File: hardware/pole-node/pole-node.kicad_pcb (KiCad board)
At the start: 2 copper layers, 50.5 x 33.5 mm, 31 parts, among them J1 Anderson, J2 RJ45, J3 Conn_01x02, J4 Conn_01x03, J5 Conn_01x03, J6 Conn_01x03, U1 AP3211, U2 MAX485E, U3 MAX485E

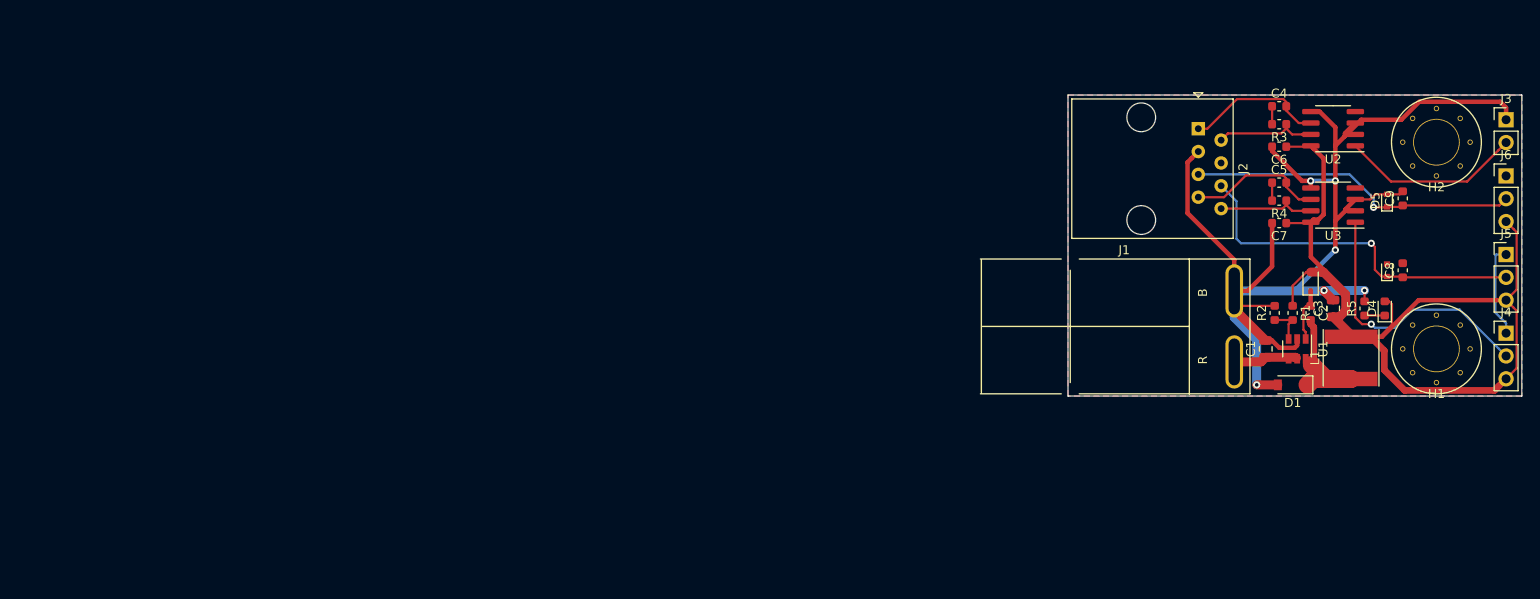
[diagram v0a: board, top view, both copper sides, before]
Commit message: Update pole node to v1.1
This adds lots of TVS diode, more decoupling, bulk caps on 5v and 12v
lines. Also adds pass-through Anderson connector.
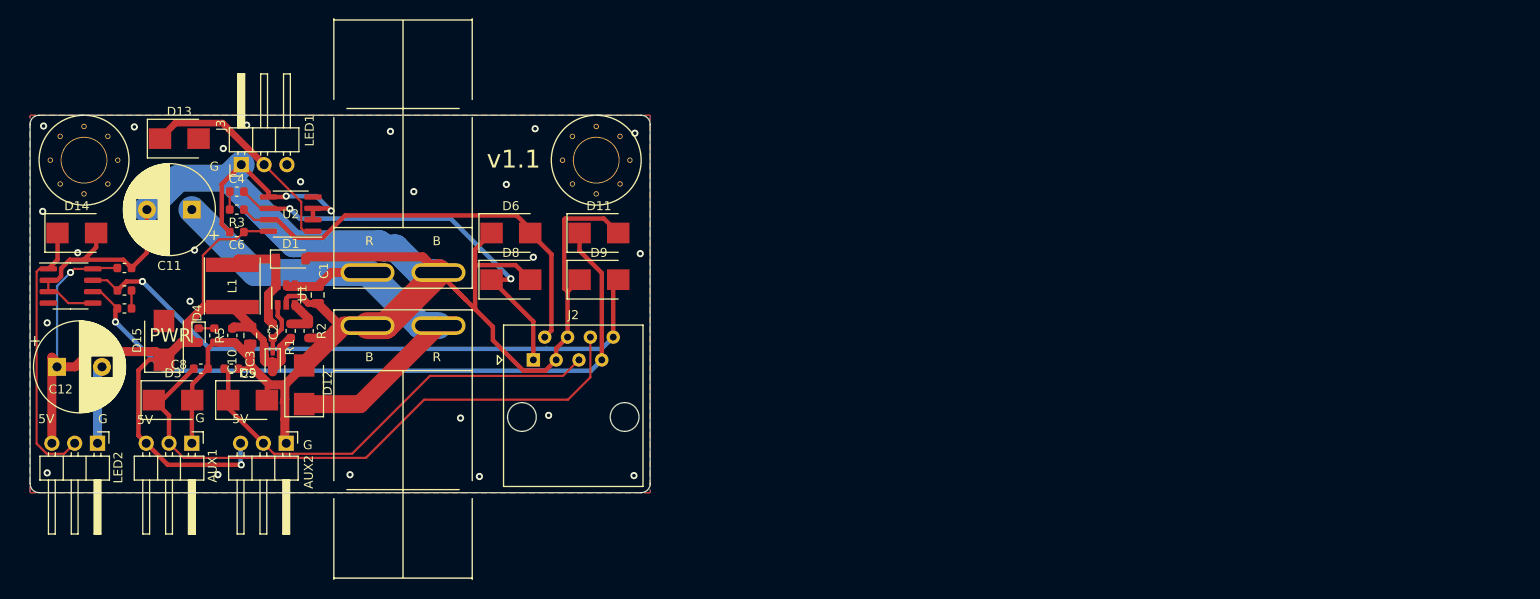
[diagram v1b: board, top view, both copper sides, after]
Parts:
- added C10: .1uF, Capacitor_SMD:C_0603_1608Metric, F.Cu at (60.0, 60.0)
- added C11: 470uF, Capacitor_THT:CP_Radial_D10.0mm_P5.00mm, F.Cu at (55.5, 46.0)
- added C12: 470uF, Capacitor_THT:CP_Radial_D10.0mm_P5.00mm, F.Cu at (40.5, 63.5)
- added D11: D_TVS_DATA, Diode_SMD:D_SMB, F.Cu at (100.8, 48.6)
- added D12: D_TVS_12V, Diode_SMD:D_SMB, F.Cu at (68.0, 65.5)
- added D13: D_TVS_5V, Diode_SMD:D_SMB, F.Cu at (54.1, 38.1)
- added D14: D_TVS_5V, Diode_SMD:D_SMB, F.Cu at (42.7, 48.6)
- added D15: D_TVS_5V, Diode_SMD:D_SMB, F.Cu at (52.4, 60.5)
- added D6: D_TVS_DATA, Diode_SMD:D_SMB, F.Cu at (91.0, 48.6)
- added D8: D_TVS_DATA, Diode_SMD:D_SMB, F.Cu at (91.0, 53.8)
- added D9: D_TVS_DATA, Diode_SMD:D_SMB, F.Cu at (100.8, 53.8)
- added J7: Anderson, homebrew:Anderson_1336G1_right_angle_bottom_two, F.Cu at (79.0, 53.0)
- D3, D5: value D_TVS -> D_TVS_5V; footprint Diode_SMD:D_SOD-523 -> Diode_SMD:D_SMB
- J1: footprint homebrew:Anderson_1337G3_right_angle_bottom_two -> homebrew:Anderson_1336G1_right_angle_bottom_two
- J3: value Conn_01x02 -> Conn_01x03; footprint Connector_PinHeader_2.54mm:PinHeader_1x02_P2.54mm_Vertical -> Connector_PinHeader_2.54mm:PinHeader_1x03_P2.54mm_Horizontal
- J4, J5, J6: footprint Connector_PinHeader_2.54mm:PinHeader_1x03_P2.54mm_Vertical -> Connector_PinHeader_2.54mm:PinHeader_1x03_P2.54mm_Horizontal
- moved J4 157.2 mm to (45.0, 72.0), turned to 270 degrees
- moved H1 152.0 mm to (43.5, 40.5)
- moved J5 147.8 mm to (55.5, 72.0), turned to 270 degrees
- moved J3 140.8 mm to (61.0, 41.0), turned to 90 degrees
- moved U3 140.8 mm to (42.0, 54.5), turned to 0 degrees
- moved J6 139.0 mm to (66.0, 72.0), turned to 270 degrees
- moved D3 135.9 mm to (53.4, 67.2), turned to 0 degrees
- moved C8 134.2 mm to (56.5, 63.7), turned to 0 degrees
- moved D4 132.0 mm to (56.2, 60.0), turned to 270 degrees
- moved C9 131.7 mm to (59.9, 63.7), turned to 0 degrees
- moved C5 129.3 mm to (48.0, 57.0), turned to 180 degrees
- moved R4 128.9 mm to (48.0, 55.0), turned to 0 degrees
- moved D5 128.7 mm to (61.7, 67.2), turned to 0 degrees
- moved C7 128.6 mm to (48.0, 52.5), turned to 0 degrees
- moved R5 128.0 mm to (58.0, 60.0), turned to 270 degrees
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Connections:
- net Net-(C1-Pad1) renamed +12V
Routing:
- net GND: track 162.9 -> 250.8 mm, vias 6 -> 26
- net LED_2_A: track 15.2 -> 77.1 mm, vias 0 -> 1
- net LED_2_B: track 10.9 -> 69.1 mm, vias 0 -> 1
- net +12V: track 7.17 -> 61.0 mm
- net LED_1_B: track 11.3 -> 47.5 mm
- net LED_1_A: track 15.6 -> 46.8 mm, vias 0 -> 2
- net PIR1: track 39.9 -> 67.2 mm, vias 1 -> 0
- net PIR2: track 36.8 -> 50.0 mm, vias 1 -> 0
- net LED_1_OUT: track 20.7 -> 24.4 mm
- net +5V: track 106.2 -> 109.9 mm, vias 0 -> 2
- net Net-(C2-Pad2): track 15.4 -> 12.5 mm
- net LED_2_OUT: track 30.8 -> 30.2 mm, vias 1 -> 0
- net Net-(D4-Pad1): track 2.25 -> 1.75 mm
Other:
- board size 50.5 x 33.5 mm -> 69 x 42 mm
- rule pad_to_mask_clearance: 0.051 -> 0
- board text added: "1"
- board text added: "12v"
- board text added: "1A"
- board text added: "1B"
- board text added: "2"
- board text added: "2A"
- board text added: "2B"
- board text added: "AUX1"
- board text added: "AUX2"
- board text added: "PWR"
- board text added: "pole-node v1.1"
- board text added: "v1.1"
- board text removed: "PIR1"
- board text removed: "PIR2"

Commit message: Pole node v1.2.
Same circuit as v1.1, but with all connectors on the same side.
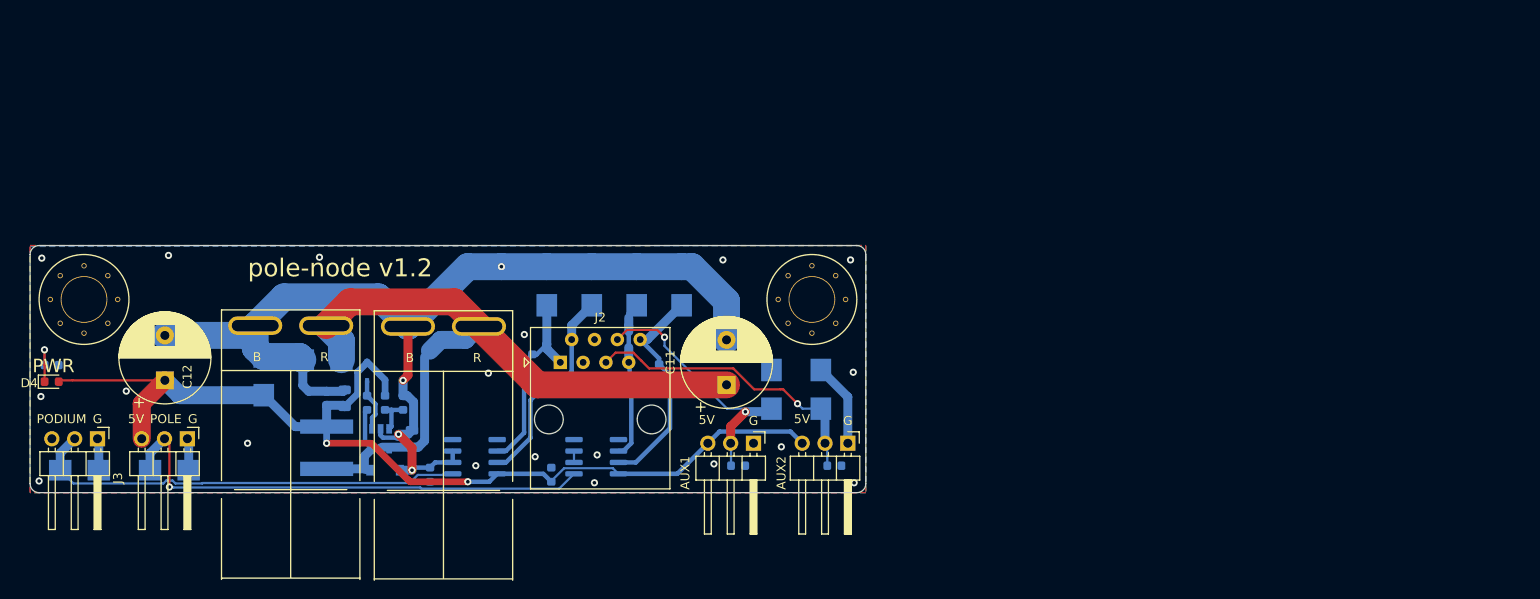
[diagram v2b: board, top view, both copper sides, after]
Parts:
- C1, C10, C2, C3, C4, C5, C6, C7, C8, C9, D1, D11, D12, D13, D14, D15, D2, D3, D5, D6, D8, D9, L1, R1, R2, R3, R4, R5, U1, U2, U3: moved to B.Cu
- moved C9 68.0 mm to (127.0, 74.5)
- moved D3 66.6 mm to (120.0, 66.0), turned to 90 degrees
- moved D5 63.8 mm to (125.5, 66.0), turned to 90 degrees
- moved C11 62.6 mm to (115.0, 65.5), turned to 90 degrees
- moved J5 62.5 mm to (118.0, 72.0)
- moved J6 62.5 mm to (128.5, 72.0)
- moved U3 61.5 mm to (100.5, 73.5)
- moved C8 60.8 mm to (116.3, 74.5)
- moved R4 60.2 mm to (107.5, 64.0), turned to 270 degrees
- moved C5 57.6 mm to (105.0, 65.0)
- moved C7 52.8 mm to (95.5, 75.5), turned to 90 degrees
- moved R3 38.9 mm to (94.2, 65.4)
- moved D13 38.5 mm to (43.0, 75.0)
- moved C4 37.9 mm to (93.4, 62.9), turned to 90 degrees
- moved C6 34.5 mm to (82.0, 75.5), turned to 90 degrees
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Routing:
- net GND: track 250.8 -> 139.4 mm, vias 26 -> 23
- net LED_2_A: track 77.1 -> 19.2 mm, vias 1 -> 0
- net LED_2_B: track 69.1 -> 24.7 mm, vias 1 -> 0
- net PIR1: track 67.2 -> 31.5 mm, vias 0 -> 2
- net LED_2_OUT: track 30.2 -> 55.5 mm, vias 0 -> 1
- net LED_1_A: track 46.8 -> 22.0 mm, vias 2 -> 0
- net LED_1_OUT: track 24.4 -> 49.2 mm
- net LED_1_B: track 47.5 -> 23.2 mm
- net PIR2: track 50.0 -> 33.6 mm, vias 0 -> 1
- net +12V: track 61.0 -> 74.9 mm
- net +5V: track 109.9 -> 120.2 mm
- net Net-(D4-Pad1): track 1.75 -> 5.28 mm, vias 0 -> 1
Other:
- board size 69 x 42 mm -> 93 x 27.5 mm
- board text added: "PODIUM"
- board text added: "POLE"
- board text added: "pole-node v1.2"
- board text removed: "LED1"
- board text removed: "LED2"
- board text removed: "pole-node v1.1"
- board text removed: "v1.1"
